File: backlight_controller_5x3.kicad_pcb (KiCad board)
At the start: 2 copper layers, 121.3 x 67.3 mm, 39 parts, among them J1 M12-5_RCPT_F, J2 M12-5_RCPT_F, J3 DB9F, J4 DB9M, P1 MINI_FIT_JR_02X03_M_RA, P2 PWR_JACK_2.5x5.5, U1 SN74ABT541BDWR, U2 SN74ABT541BDWR

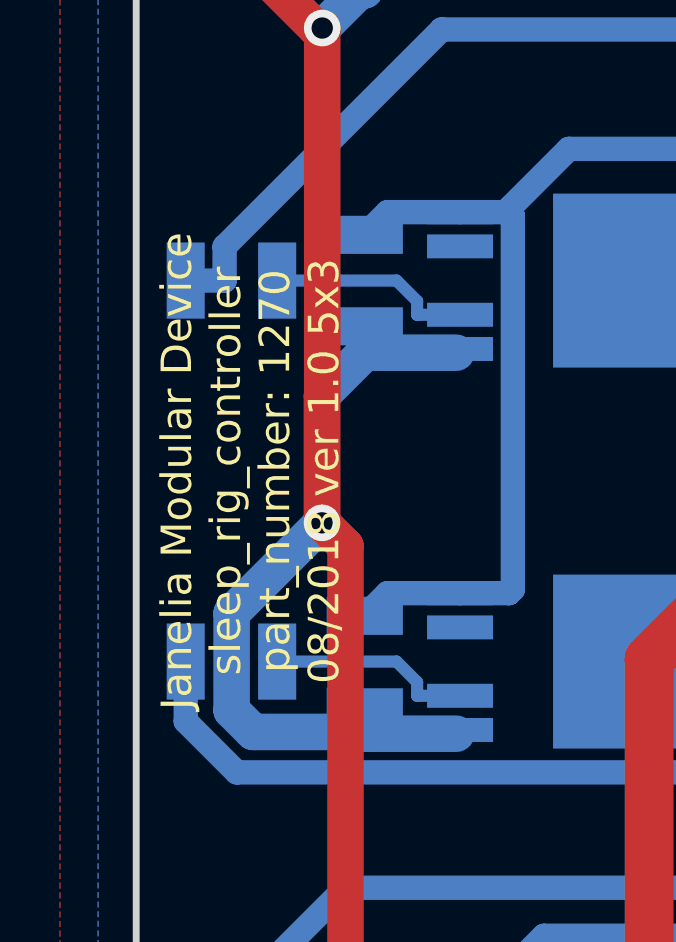
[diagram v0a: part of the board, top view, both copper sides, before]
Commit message: sleep_rig -> backlight.
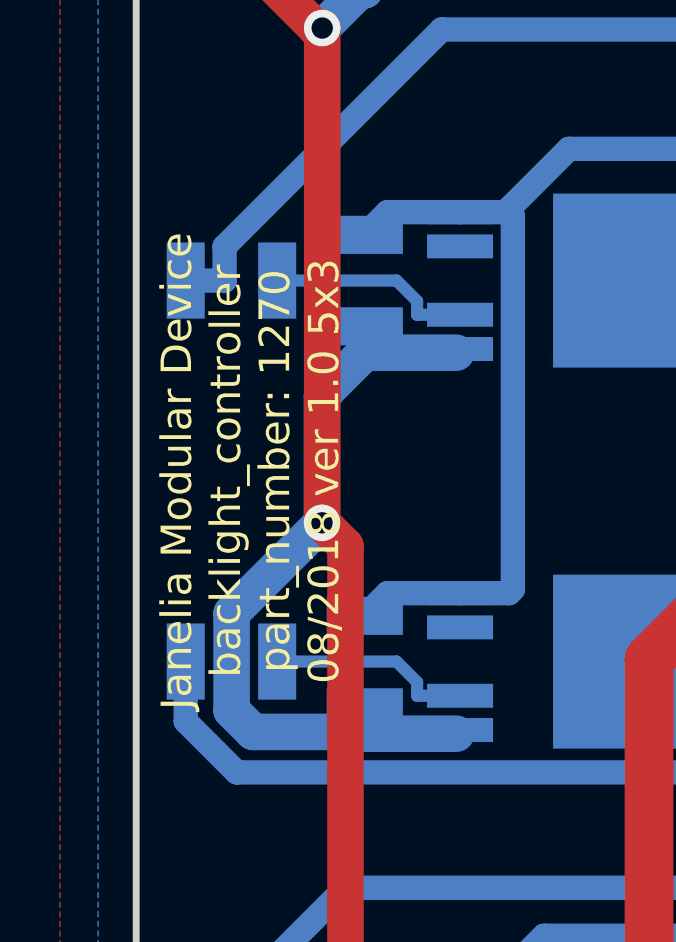
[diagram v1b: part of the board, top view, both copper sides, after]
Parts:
- C1, C2, C3, C4, C5, C6, R1, R2, R3, R4, R5, R6, R7, R8: footprint sleep_rig_controller_5x3:SM1210 -> backlight_controller_5x3:SM1210
- D1: footprint sleep_rig_controller_5x3:CFP15 -> backlight_controller_5x3:CFP15
- HPS1, HPS2, HPS3, HPS4: footprint sleep_rig_controller_5x3:PG-TO252-5-11 -> backlight_controller_5x3:PG-TO252-5-11
- J1, J2: footprint sleep_rig_controller_5x3:M12-5_RCPT_F -> backlight_controller_5x3:M12-5_RCPT_F
- J3: footprint sleep_rig_controller_5x3:DB9F -> backlight_controller_5x3:DB9F
- J4: footprint sleep_rig_controller_5x3:DB9M -> backlight_controller_5x3:DB9M
- L1: footprint sleep_rig_controller_5x3:LED_555-3XXX_R -> backlight_controller_5x3:LED_555-3XXX_R
- L10, L11, L2, L3, L4, L5, L6, L7, L8, L9: footprint sleep_rig_controller_5x3:LED_555-3XXX_G -> backlight_controller_5x3:LED_555-3XXX_G
- MDB1: footprint sleep_rig_controller_5x3:MODULAR_DEVICE_BASE_5X3_MALE -> backlight_controller_5x3:MODULAR_DEVICE_BASE_5X3_MALE
- P1: footprint sleep_rig_controller_5x3:MINI-FIT-JR_02X03_M_RA -> backlight_controller_5x3:MINI-FIT-JR_02X03_M_RA
- P2: footprint sleep_rig_controller_5x3:DCJACK_2PIN_HIGHCURRENT -> backlight_controller_5x3:DCJACK_2PIN_HIGHCURRENT
- U1, U2: footprint sleep_rig_controller_5x3:SOIC_20 -> backlight_controller_5x3:SOIC_20
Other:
- board text added: "Janelia Modular Device backlight_controller part_number: 1270 08/2018 ver 1.0 5x3"
- board text removed: "Janelia Modular Device sleep_rig_controller part_number: 1270 08/2018 ver 1.0 5x3"
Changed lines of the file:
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@@
   (page A4)
   (title_block
-    (title sleep_rig_controller_5x3)
+    (title backlight_controller_5x3)
     (rev 1.0)
   )
@@
     (add_net VAA)
   )
-  (module sleep_rig_controller_5x3:SM1210 (layer B.Cu)
+  (module backlight_controller_5x3:SM1210 (layer B.Cu)
     (at 133.35 111.125)
     (tags "CMS SM")
@@
     )
   )
-  (module sleep_rig_controller_5x3:DCJACK_2PIN_HIGHCURRENT (layer F.Cu)
+  (module backlight_controller_5x3:DCJACK_2PIN_HIGHCURRENT (layer F.Cu)
     (at 190.5 118.11 270)
     (fp_text reference P2 (at -6.985 2.54) (layer F.SilkS)
@@
     (pad "" thru_hole circle (at 0 2.9972 270) (size 1.9304 1.9304) (drill 1.6002) (layers *.Cu *.Mask))
   )
-  (module sleep_rig_controller_5x3:MINI-FIT-JR_02X03_M_RA (layer F.Cu)
+  (module backlight_controller_5x3:MINI-FIT-JR_02X03_M_RA (layer F.Cu)
     (at 187.96 92.71 90)
     (fp_text reference P1 (at -8.255 0 180) (layer F.SilkS)
@@
     (pad "" thru_hole circle (at 4.2 0 90) (size 4 4) (drill 3) (layers *.Cu *.Mask))
   )
-  (module sleep_rig_controller_5x3:MODULAR_DEVICE_BASE_5X3_MALE (layer F.Cu)
+  (module backlight_controller_5x3:MODULAR_DEVICE_BASE_5X3_MALE (layer F.Cu)
     (at 91.44 105.41)
     (fp_text reference MDB1 (at 0 0) (layer F.SilkS) hide
@@
       (net 2 GND))
   )
-  (module sleep_rig_controller_5x3:CFP15 (layer B.Cu)
+  (module backlight_controller_5x3:CFP15 (layer B.Cu)
     (at 81.915 79.375 90)
     (fp_text reference D1 (at 0 -4.6 90) (layer B.SilkS)
@@
       (net 3 VDD) (solder_mask_margin 0.1) (clearance 0.1))
   )
-  (module sleep_rig_controller_5x3:SM1210 (layer B.Cu)
+  (module backlight_controller_5x3:SM1210 (layer B.Cu)
     (at 111.76 113.665)
     (tags "CMS SM")
@@
     )
   )
-  (module sleep_rig_controller_5x3:SM1210 (layer B.Cu)
+  (module backlight_controller_5x3:SM1210 (layer B.Cu)
     (at 143.51 113.665)
     (tags "CMS SM")
@@
     )
   )
-  (module sleep_rig_controller_5x3:SM1210 (layer B.Cu)
+  (module backlight_controller_5x3:SM1210 (layer B.Cu)
     (at 77.47 86.36 90)
     (tags "CMS SM")
@@
     )
   )
-  (module sleep_rig_controller_5x3:SM1210 (layer B.Cu)
+  (module backlight_controller_5x3:SM1210 (layer B.Cu)
     (at 77.47 99.06 90)
     (tags "CMS SM")
@@
     )
   )
-  (module sleep_rig_controller_5x3:SM1210 (layer B.Cu)
+  (module backlight_controller_5x3:SM1210 (layer B.Cu)
     (at 77.47 111.76 90)
     (tags "CMS SM")
@@
     )
   )
-  (module sleep_rig_controller_5x3:SM1210 (layer B.Cu)
+  (module backlight_controller_5x3:SM1210 (layer B.Cu)
     (at 77.47 124.46 90)
     (tags "CMS SM")
@@
     )
   )
-  (module sleep_rig_controller_5x3:PG-TO252-5-11 (layer B.Cu)
+  (module backlight_controller_5x3:PG-TO252-5-11 (layer B.Cu)
     (at 80.645 86.36 90)
     (fp_text reference HPS1 (at -4.445 5.1) (layer B.SilkS)
@@
       (net 2 GND))
   )
-  (module sleep_rig_controller_5x3:PG-TO252-5-11 (layer B.Cu)
+  (module backlight_controller_5x3:PG-TO252-5-11 (layer B.Cu)
     (at 80.645 99.06 90)
     (fp_text reference HPS2 (at -4.445 5.1) (layer B.SilkS)
@@
       (net 2 GND))
   )
-  (module sleep_rig_controller_5x3:PG-TO252-5-11 (layer B.Cu)
+  (module backlight_controller_5x3:PG-TO252-5-11 (layer B.Cu)
     (at 80.645 111.76 90)
     (fp_text reference HPS3 (at -4.445 5.1) (layer B.SilkS)
@@
       (net 2 GND))
   )
-  (module sleep_rig_controller_5x3:PG-TO252-5-11 (layer B.Cu)
+  (module backlight_controller_5x3:PG-TO252-5-11 (layer B.Cu)
     (at 80.645 124.46 90)
     (fp_text reference HPS4 (at -4.445 5.08) (layer B.SilkS)
@@
       (net 2 GND))
   )
-  (module sleep_rig_controller_5x3:DB9F (layer F.Cu)
+  (module backlight_controller_5x3:DB9F (layer F.Cu)
     (at 120.65 92.71)
     (fp_text reference J3 (at 0 7.62) (layer F.SilkS)
@@
       (net 18 /BUZZER))
   )
-  (module sleep_rig_controller_5x3:DB9M (layer F.Cu)
+  (module backlight_controller_5x3:DB9M (layer F.Cu)
     (at 120.65 118.11)
     (fp_text reference J4 (at 0 -7.62) (layer F.SilkS)
@@
       (net 2 GND))
   )
-  (module sleep_rig_controller_5x3:M12-5_RCPT_F (layer F.Cu)
+  (module backlight_controller_5x3:M12-5_RCPT_F (layer F.Cu)
     (at 152.4 92.71)
     (fp_text reference J1 (at 0 10.16) (layer F.SilkS)
@@
       (net 4 VAA))
   )
-  (module sleep_rig_controller_5x3:M12-5_RCPT_F (layer F.Cu)
+  (module backlight_controller_5x3:M12-5_RCPT_F (layer F.Cu)
     (at 152.4 118.11)
     (fp_text reference J2 (at 0 -10.16) (layer F.SilkS)
@@
       (net 4 VAA))
   )
-  (module sleep_rig_controller_5x3:SM1210 (layer B.Cu)
+  (module backlight_controller_5x3:SM1210 (layer B.Cu)
     (at 73.025 85.725 180)
     (tags "CMS SM")
@@
     )
   )
-  (module sleep_rig_controller_5x3:SM1210 (layer B.Cu)
+  (module backlight_controller_5x3:SM1210 (layer B.Cu)
     (at 73.025 99.06 180)
     (tags "CMS SM")
@@
     )
   )
-  (module sleep_rig_controller_5x3:SM1210 (layer B.Cu)
+  (module backlight_controller_5x3:SM1210 (layer B.Cu)
     (at 73.025 111.76 180)
     (tags "CMS SM")
@@
     )
   )
-  (module sleep_rig_controller_5x3:SM1210 (layer B.Cu)
+  (module backlight_controller_5x3:SM1210 (layer B.Cu)
     (at 73.025 124.46 180)
     (tags "CMS SM")
@@
     )
   )
-  (module sleep_rig_controller_5x3:SM1210 (layer B.Cu)
+  (module backlight_controller_5x3:SM1210 (layer B.Cu)
     (at 133.35 99.695)
     (tags "CMS SM")
@@
     )
   )
-  (module sleep_rig_controller_5x3:SM1210 (layer B.Cu)
+  (module backlight_controller_5x3:SM1210 (layer B.Cu)
     (at 133.35 103.505)
     (tags "CMS SM")
@@
     )
   )
-  (module sleep_rig_controller_5x3:SM1210 (layer B.Cu)
+  (module backlight_controller_5x3:SM1210 (layer B.Cu)
     (at 133.35 107.315)
     (tags "CMS SM")
@@
     )
   )
-  (module sleep_rig_controller_5x3:SOIC_20 (layer B.Cu)
+  (module backlight_controller_5x3:SOIC_20 (layer B.Cu)
     (at 111.76 105.41 180)
     (fp_text reference U1 (at 0 7.62 180) (layer B.SilkS)
@@
       (net 1 VEE) (solder_mask_margin 0.07) (clearance 0.07))
   )
-  (module sleep_rig_controller_5x3:SOIC_20 (layer B.Cu)
+  (module backlight_controller_5x3:SOIC_20 (layer B.Cu)
     (at 143.51 105.41 180)
     (fp_text reference U2 (at 0 7.62 180) (layer B.SilkS)
@@
       (net 1 VEE) (solder_mask_margin 0.07) (clearance 0.07))
   )
-  (module sleep_rig_controller_5x3:LED_555-3XXX_R (layer F.Cu)
+  (module backlight_controller_5x3:LED_555-3XXX_R (layer F.Cu)
     (at 166.37 105.41)
     (fp_text reference L1 (at 0 -4.445 180) (layer F.SilkS)
@@
       (net 2 GND))
   )
-  (module sleep_rig_controller_5x3:LED_555-3XXX_G (layer F.Cu)
+  (module backlight_controller_5x3:LED_555-3XXX_G (layer F.Cu)
     (at 93.345 86.995)
     (fp_text reference L2 (at -1.905 0 90) (layer F.SilkS)
@@
       (net 28 /C_0))
   )
-  (module sleep_rig_controller_5x3:LED_555-3XXX_G (layer F.Cu)
+  (module backlight_controller_5x3:LED_555-3XXX_G (layer F.Cu)
     (at 95.885 86.995)
     (fp_text reference L3 (at 0 4.5) (layer F.SilkS) hide
@@
       (net 2 GND))
   )
-  (module sleep_rig_controller_5x3:LED_555-3XXX_G (layer F.Cu)
+  (module backlight_controller_5x3:LED_555-3XXX_G (layer F.Cu)
     (at 98.425 86.995)
     (fp_text reference L4 (at 0 4.5) (layer F.SilkS) hide
@@
       (net 30 /C_2))
   )
-  (module sleep_rig_controller_5x3:LED_555-3XXX_G (layer F.Cu)
+  (module backlight_controller_5x3:LED_555-3XXX_G (layer F.Cu)
     (at 100.965 86.995)
     (fp_text reference L5 (at 1.905 0 90) (layer F.SilkS)
@@
       (net 2 GND))
   )
-  (module sleep_rig_controller_5x3:LED_555-3XXX_G (layer F.Cu)
+  (module backlight_controller_5x3:LED_555-3XXX_G (layer F.Cu)
     (at 93.345 123.825)
     (fp_text reference L6 (at -1.905 0 90) (layer F.SilkS)
@@
       (net 32 /C_8))
   )
-  (module sleep_rig_controller_5x3:LED_555-3XXX_G (layer F.Cu)
+  (module backlight_controller_5x3:LED_555-3XXX_G (layer F.Cu)
     (at 95.885 123.825)
     (fp_text reference L7 (at 0 4.5) (layer F.SilkS) hide
@@
       (net 33 /C_9))
   )
-  (module sleep_rig_controller_5x3:LED_555-3XXX_G (layer F.Cu)
+  (module backlight_controller_5x3:LED_555-3XXX_G (layer F.Cu)
     (at 98.425 123.825)
     (fp_text reference L8 (at 0 4.5) (layer F.SilkS) hide
@@
       (net 2 GND))
   )
-  (module sleep_rig_controller_5x3:LED_555-3XXX_G (layer F.Cu)
+  (module backlight_controller_5x3:LED_555-3XXX_G (layer F.Cu)
     (at 100.965 123.825)
     (fp_text reference L9 (at 1.905 0 90) (layer F.SilkS)
@@
       (net 2 GND))
   )
-  (module sleep_rig_controller_5x3:LED_555-3XXX_G (layer F.Cu)
+  (module backlight_controller_5x3:LED_555-3XXX_G (layer F.Cu)
     (at 141.605 86.995)
     (fp_text reference L10 (at 1.905 0 90) (layer F.SilkS)
@@
       (net 2 GND))
   )
-  (module sleep_rig_controller_5x3:LED_555-3XXX_G (layer F.Cu)
+  (module backlight_controller_5x3:LED_555-3XXX_G (layer F.Cu)
     (at 141.605 123.825)
     (fp_text reference L11 (at 1.905 -0.635 90) (layer F.SilkS)
@@
     (effects (font (size 1.016 1.016) (thickness 0.1905)))
   )
-  (gr_text "Janelia Modular Device\nsleep_rig_controller\npart_number: 1270\n08/2018 ver 1.0 5x3" (at 73.66 105.41 90) (layer F.SilkS)
+  (gr_text "Janelia Modular Device\nbacklight_controller\npart_number: 1270\n08/2018 ver 1.0 5x3" (at 73.66 105.41 90) (layer F.SilkS)
     (effects (font (size 1.016 1.016) (thickness 0.254)))
   )

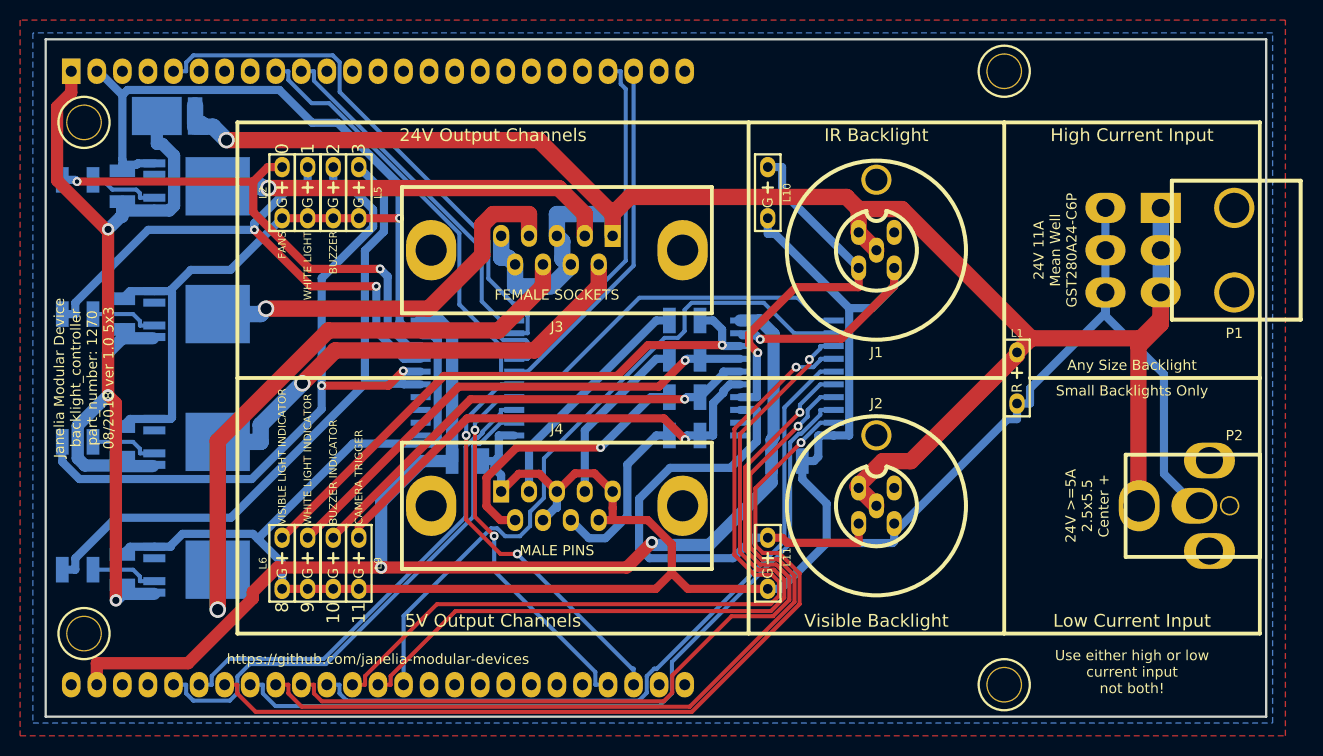
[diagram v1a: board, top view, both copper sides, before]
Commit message: Reorganized schematics.
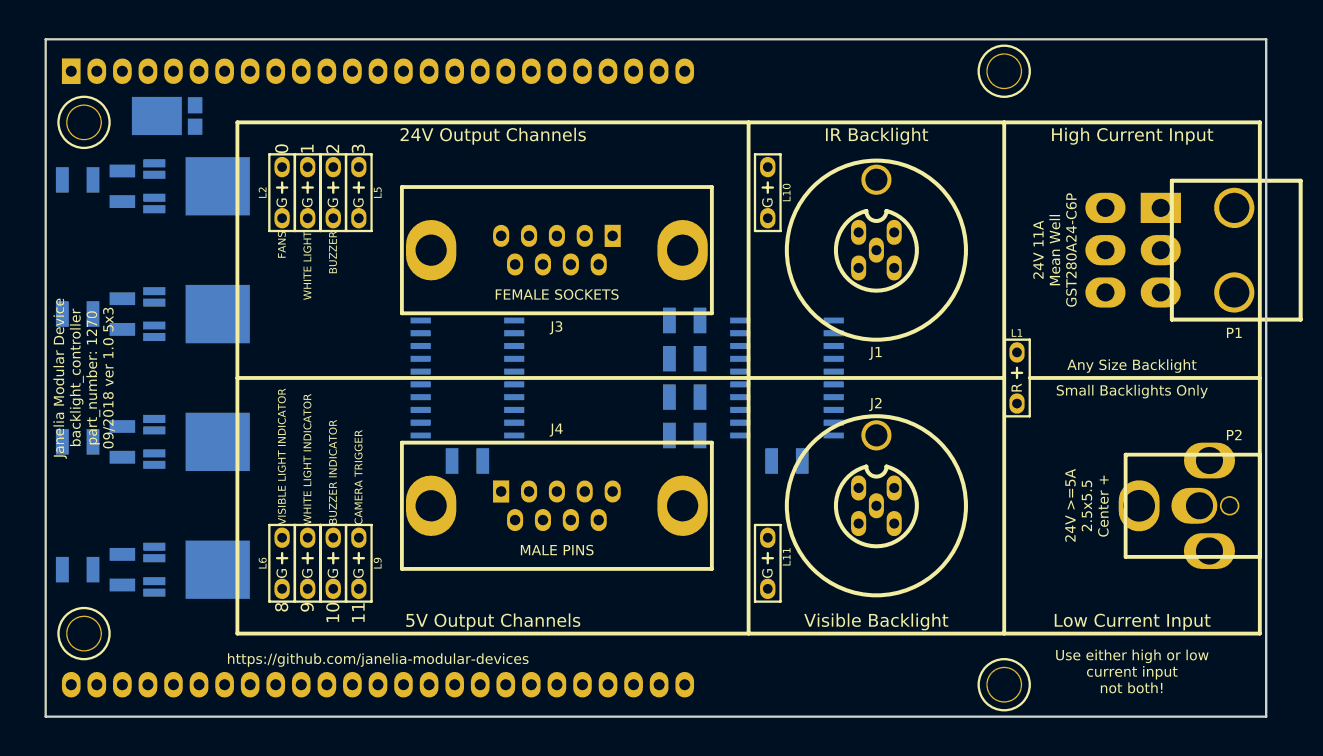
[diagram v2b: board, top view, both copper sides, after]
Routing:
- net GND: track 406.8 -> 0.00 mm, vias 2 -> 0
- net VAA: track 201.8 -> 0.00 mm, vias 1 -> 0
- net VEE: track 127.5 -> 0.00 mm, vias 2 -> 0
- net VDD: track 106.3 -> 0.00 mm, vias 3 -> 0
- net /CHANNEL_15: track 88.0 -> 0.00 mm, vias 1 -> 0
- net /CHANNEL_13: track 84.6 -> 0.00 mm, vias 1 -> 0
- net /CHANNEL_12: track 83.5 -> 0.00 mm, vias 1 -> 0
- net /~ENABLE: track 82.7 -> 0.00 mm
- net /CHANNEL_14: track 79.6 -> 0.00 mm
- net /CHANNEL_10: track 78.8 -> 0.00 mm, vias 1 -> 0
- net /CHANNEL_9: track 76.9 -> 0.00 mm, vias 1 -> 0
- net /CHANNEL_11: track 73.8 -> 0.00 mm
- net /C_2: track 70.5 -> 0.00 mm, vias 2 -> 0
- net /CHANNEL_8: track 68.8 -> 0.00 mm
- net /C_3: track 67.3 -> 0.00 mm
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- removed copper zone on B.Cu, net GND
- removed copper zone on F.Cu, net VAA
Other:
- board text added: "Janelia Modular Device backlight_controller part_number: 1270 09/2018 ver 1.0 5x3"
- board text removed: "Janelia Modular Device backlight_controller part_number: 1270 08/2018 ver 1.0 5x3"
